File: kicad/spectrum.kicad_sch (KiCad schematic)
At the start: 258 parts, among them J1 SUPPLY, J2 Input, J3 Output, SW1 POWER, SW2 RIGHT SOURCE, SW3 LEFT SOURCE, U1 LM833, U10 LM833, U11 LM833, U12 LM833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

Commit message: Isolation transformer and resistor tweaks
- Audio isolation transformer to fix ground loop hum.
- Changed preamp Ri and mixer Rf to work compensate
  for transfomer effects.
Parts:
- added C51, C52: 0.1uF, Capacitor_THT:C_Disc_D4.3mm_W1.9mm_P5.00mm, symbol Device:C_Small
- added T1, T2: SP-70, symbol Device:Transformer_1P_1S
- R1, R126: value 1K -> 6.2K
- R54, R73: value 10K -> 51K
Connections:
- net GNDREF: now also C51.1, C52.1, T1.3 (SA), T2.4 (SB); no longer J2.S
- net Vin_L: now also T2.3 (SA); no longer J2.T
- net Vin_R: now also T1.4 (SB); no longer J2.R
- net at C50.2, R126.2: now also C52.2
- net at C1.2, R1.2: now also C51.2
- new net: J2.R, T1.1 (AA)
- new net: J2.S, T1.2 (AB), T2.1 (AA)
- new net: J2.T, T2.2 (AB)
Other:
- moved on the sheet: C1, C50, J2, TP2, TP27

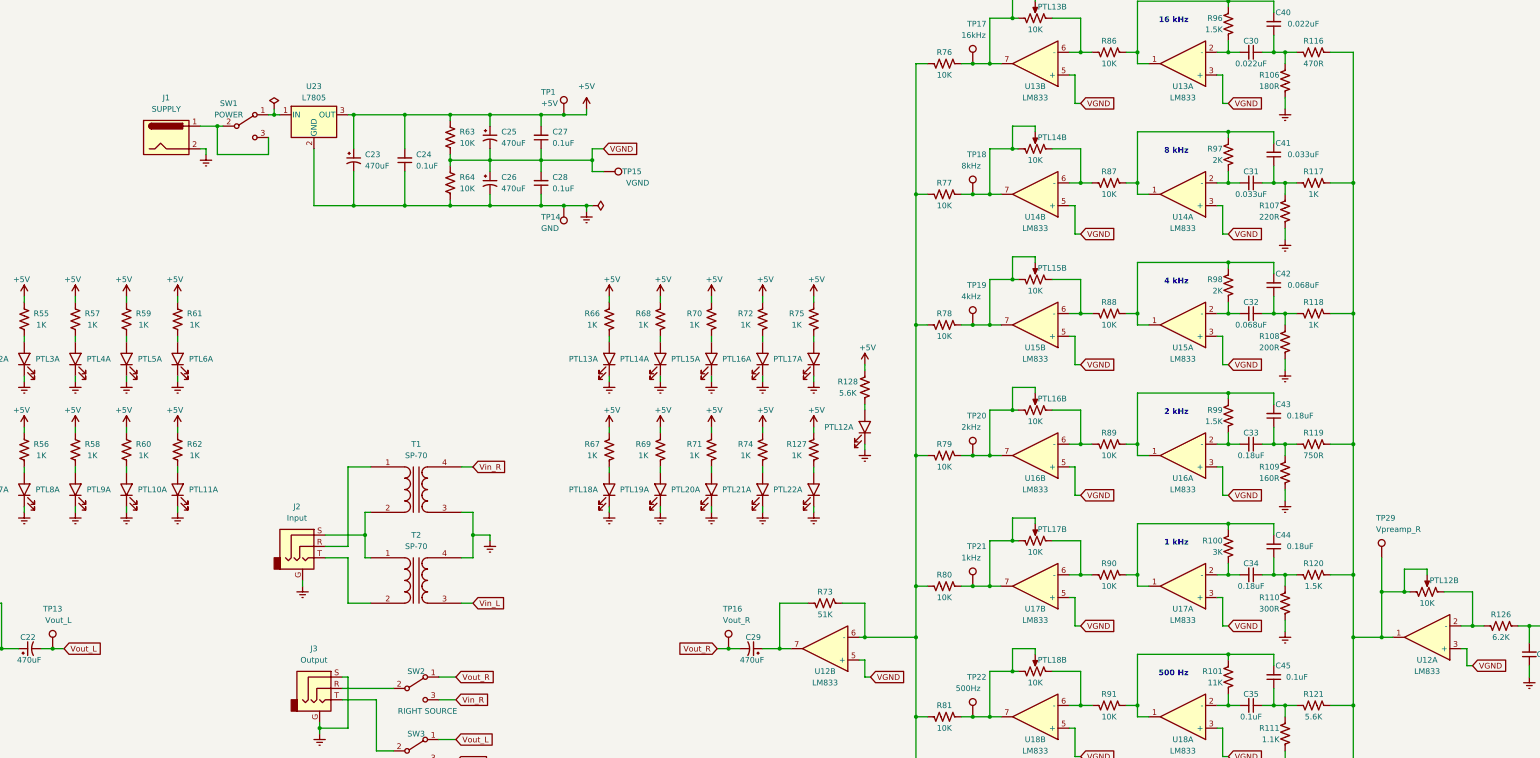
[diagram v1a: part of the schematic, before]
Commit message: Finish component layout and add extra 7805
- Extra 7805 needed for heat dissipation
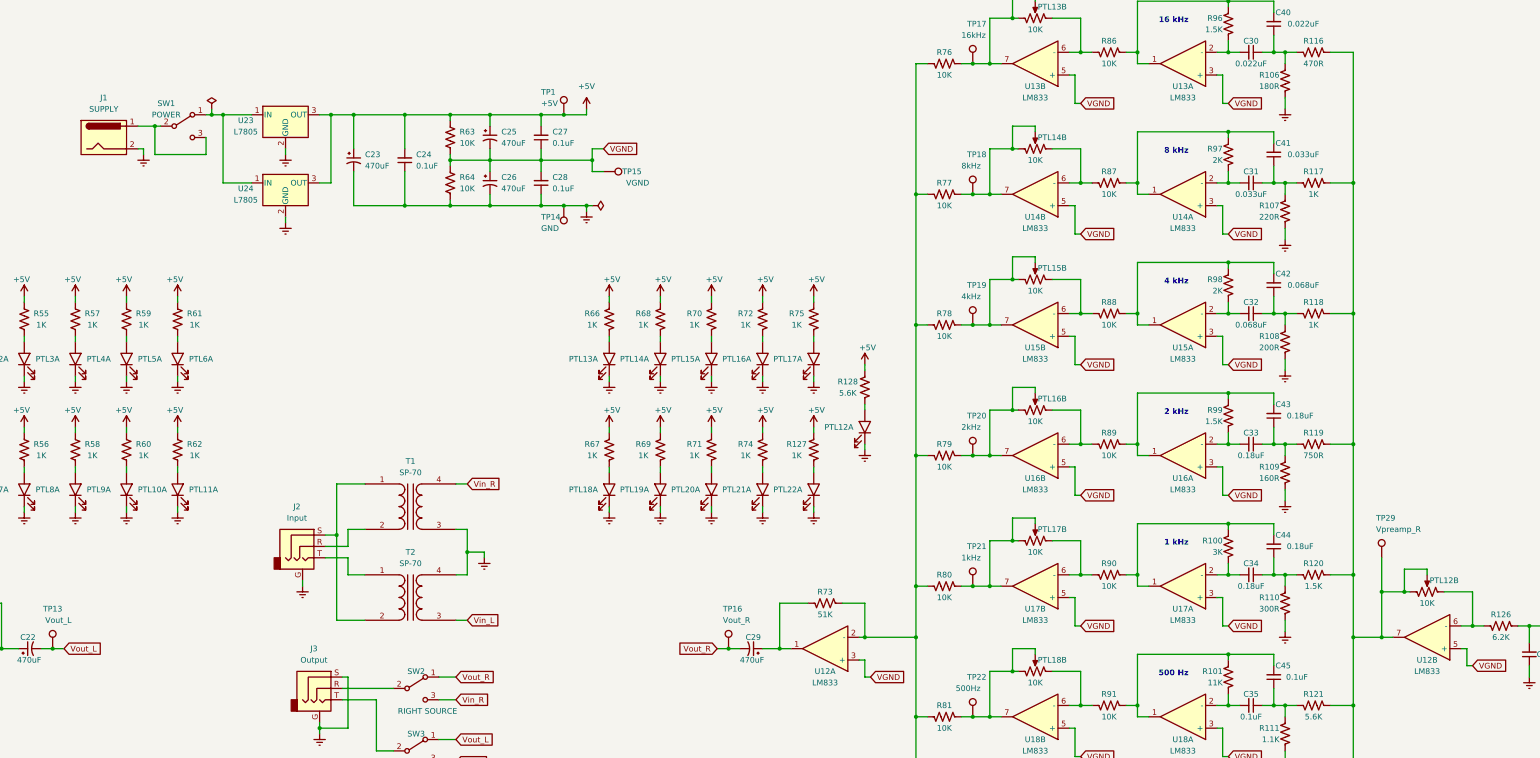
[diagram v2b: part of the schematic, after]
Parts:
- added U24: L7805, Package_TO_SOT_THT:TO-220-3_Vertical, symbol Regulator_Linear:L7805
- T1, T2: footprint (none) -> Triad_Magnetics_SP-70:SP70
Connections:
- net +5V: now also U24.3 (OUT)
- net GNDREF: now also U24.2 (GND)
- net VGND: now also U12.3 (+), U12.5 (+); no longer U12.3 (+), U12.5 (+)
- net at PTL12.2, PTL12.3, R116.2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: now also U12.7; no longer U12.1
- net at R73.2, R76.1, R77.1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: now also U12.2 (-); no longer U12.6 (-)
- net at J2.R: now also T1.2 (AB); no longer T1.1 (AA)
- net at T2.2 (AB): now also J2.S, T1.1 (AA); no longer J2.T
- net at PTL12.1, R126.1: now also U12.6 (-); no longer U12.2 (-)
- net at C29.1, R73.1: now also U12.1; no longer U12.7
- net at SW1.1 (A), U23.1 (IN): now also U24.1 (IN)
- new net: J2.T, T2.1 (AA)
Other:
- moved on the sheet: J1, SW1, T1, T2, U23

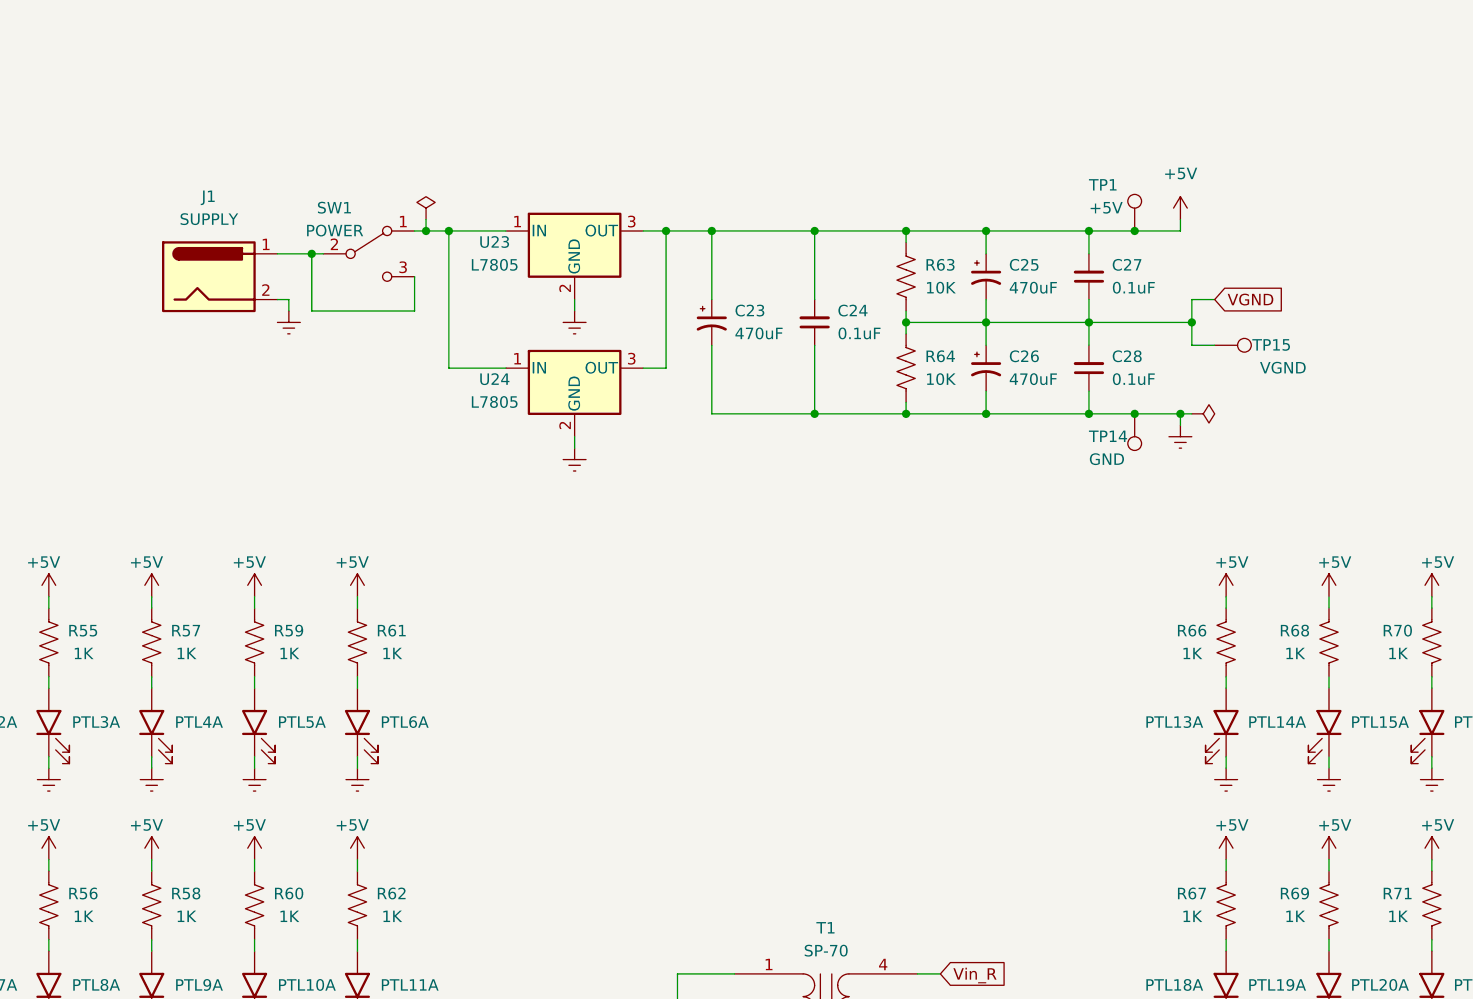
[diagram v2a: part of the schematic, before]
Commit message: Clean up board traces and use single L7805
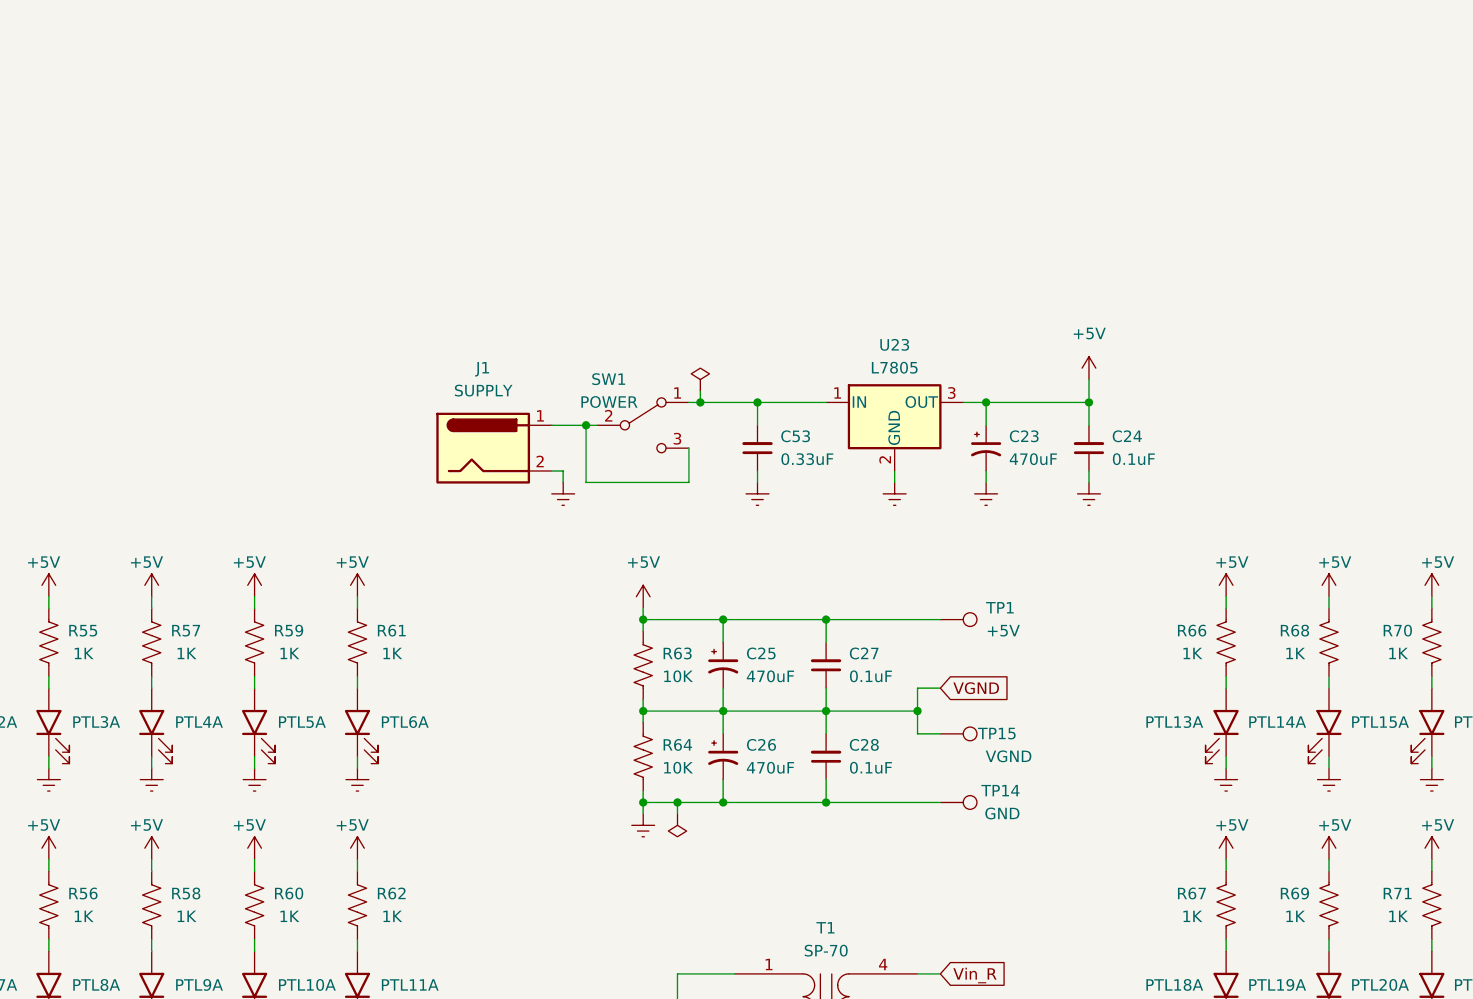
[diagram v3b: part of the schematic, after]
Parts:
- removed U24: L7805, Package_TO_SOT_THT:TO-220-3_Vertical, symbol Regulator_Linear:L7805
- added C53: 0.33uF, Capacitor_THT:C_Disc_D4.3mm_W1.9mm_P5.00mm, symbol Device:C_Small
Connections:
- net GNDREF: now also C53.1
- net at SW1.1 (A), U23.1 (IN): now also C53.2
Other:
- moved on the sheet: C23, C24, C25, C26, C27, C28, J1, R63, R64, SW1, TP1, TP14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

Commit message: Add output resistor to cut out noise
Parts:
- added R129, R130: 470R, Resistor_THT:R_Axial_DIN0207_L6.3mm_D2.5mm_P7.62mm_Horizontal, symbol Device:R_US
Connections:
- net Vout_L: now also R129.2; no longer C22.2
- net Vout_R: now also R130.1; no longer C29.2
- new net: C22.2, R129.1
- new net: C29.2, R130.2
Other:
- moved on the sheet: TP13, TP16
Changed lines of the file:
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@@
   (junction (at 303.53 153.67) (diameter 0) (color 0 0 0 0)
   )
+  (junction (at 233.68 209.55) (diameter 0) (color 0 0 0 0)
+  )
   (junction (at 496.57 163.83) (diameter 0) (color 0 0 0 0)
   )
@@
   (junction (at 132.08 222.25) (diameter 0) (color 0 0 0 0)
   )
-  (junction (at 374.65 209.55) (diameter 0) (color 0 0 0 0)
-  )
   (junction (at 144.78 280.67) (diameter 0) (color 0 0 0 0)
   )
@@
   (junction (at 283.21 143.51) (diameter 0) (color 0 0 0 0)
   )
-  (junction (at 223.52 209.55) (diameter 0) (color 0 0 0 0)
-  )
   (junction (at 466.09 163.83) (diameter 0) (color 0 0 0 0)
   )
@@
   (junction (at 57.15 204.47) (diameter 0) (color 0 0 0 0)
   )
+  (junction (at 364.49 209.55) (diameter 0) (color 0 0 0 0)
+  )
   (junction (at 433.07 224.79) (diameter 0) (color 0 0 0 0)
   )
@@
     (stroke (width 0) (type default) (color 0 0 0 0))
   )
+  (wire (pts (xy 233.68 209.55) (xy 231.14 209.55))
+    (stroke (width 0) (type default) (color 0 0 0 0))
+  )
   (wire (pts (xy 293.37 203.2) (xy 287.02 203.2))
     (stroke (width 0) (type default) (color 0 0 0 0))
@@
     (stroke (width 0) (type default) (color 0 0 0 0))
   )
-  (wire (pts (xy 374.65 209.55) (xy 372.11 209.55))
-    (stroke (width 0) (type default) (color 0 0 0 0))
-  )
   (wire (pts (xy 146.05 175.26) (xy 144.78 175.26))
     (stroke (width 0) (type default) (color 0 0 0 0))
@@
     (stroke (width 0) (type default) (color 0 0 0 0))
   )
-  (wire (pts (xy 220.98 209.55) (xy 223.52 209.55))
-    (stroke (width 0) (type default) (color 0 0 0 0))
-  )
   (wire (pts (xy 429.26 341.63) (xy 426.72 341.63))
     (stroke (width 0) (type default) (color 0 0 0 0))
@@
     (stroke (width 0) (type default) (color 0 0 0 0))
   )
+  (wire (pts (xy 364.49 209.55) (xy 361.95 209.55))
+    (stroke (width 0) (type default) (color 0 0 0 0))
+  )
   (wire (pts (xy 443.23 63.5) (xy 438.15 63.5))
     (stroke (width 0) (type default) (color 0 0 0 0))
@@
     (stroke (width 0) (type default) (color 0 0 0 0))
   )
+  (wire (pts (xy 364.49 209.55) (xy 367.03 209.55))
+    (stroke (width 0) (type default) (color 0 0 0 0))
+  )
   (wire (pts (xy 365.76 274.32) (xy 365.76 276.86))
     (stroke (width 0) (type default) (color 0 0 0 0))
@@
     (stroke (width 0) (type default) (color 0 0 0 0))
   )
+  (wire (pts (xy 233.68 209.55) (xy 236.22 209.55))
+    (stroke (width 0) (type default) (color 0 0 0 0))
+  )
   (wire (pts (xy 228.6 177.8) (xy 228.6 179.07))
     (stroke (width 0) (type default) (color 0 0 0 0))
@@
     (stroke (width 0) (type default) (color 0 0 0 0))
   )
-  (wire (pts (xy 223.52 209.55) (xy 226.06 209.55))
-    (stroke (width 0) (type default) (color 0 0 0 0))
-  )
   (wire (pts (xy 83.82 251.46) (xy 88.9 251.46))
     (stroke (width 0) (type default) (color 0 0 0 0))
@@
     (stroke (width 0) (type default) (color 0 0 0 0))
   )
+  (wire (pts (xy 374.65 209.55) (xy 377.19 209.55))
+    (stroke (width 0) (type default) (color 0 0 0 0))
+  )
   (wire (pts (xy 439.42 185.42) (xy 438.15 185.42))
     (stroke (width 0) (type default) (color 0 0 0 0))
@@
     (stroke (width 0) (type default) (color 0 0 0 0))
   )
-  (wire (pts (xy 377.19 209.55) (xy 374.65 209.55))
-    (stroke (width 0) (type default) (color 0 0 0 0))
-  )
   (wire (pts (xy 142.24 251.46) (xy 144.78 251.46))
     (stroke (width 0) (type default) (color 0 0 0 0))
@@
     (stroke (width 0) (type default) (color 0 0 0 0))
   )
+  (wire (pts (xy 220.98 209.55) (xy 223.52 209.55))
+    (stroke (width 0) (type default) (color 0 0 0 0))
+  )
   (wire (pts (xy 435.61 224.79) (xy 433.07 224.79))
     (stroke (width 0) (type default) (color 0 0 0 0))
@@
     )
   )
-  (global_label "Vout_L" (shape input) (at 226.06 209.55 0) (fields_autoplaced)
+  (global_label "Vout_L" (shape input) (at 236.22 209.55 0) (fields_autoplaced)
     (effects (font (size 1.27 1.27)) (justify left))
-    (property "Intersheet References" "${INTERSHEET_REFS}" (id 0) (at 234.5812 209.4706 0)
+    (property "Intersheet References" "${INTERSHEET_REFS}" (id 0) (at 244.7412 209.4706 0)
       (effects (font (size 1.27 1.27)) (justify left) hide)
     )
@@
     )
   )
-  (global_label "Vout_R" (shape input) (at 372.11 209.55 180) (fields_autoplaced)
+  (global_label "Vout_R" (shape input) (at 361.95 209.55 180) (fields_autoplaced)
     (effects (font (size 1.27 1.27)) (justify right))
-    (property "Intersheet References" "${INTERSHEET_REFS}" (id 0) (at 363.3469 209.4706 0)
+    (property "Intersheet References" "${INTERSHEET_REFS}" (id 0) (at 353.1869 209.4706 0)
       (effects (font (size 1.27 1.27)) (justify right) hide)
     )
@@
     (pin "2")
   )
+  (symbol (lib_id "Device:R_US") (at 370.84 209.55 90) (unit 1)
+    (in_bom yes) (on_board yes)
+    (property "Reference" "R130" (id 0) (at 370.84 207.01 90))
+    (property "Value" "470R" (id 1) (at 370.84 212.09 90))
+    (property "Footprint" "Resistor_THT:R_Axial_DIN0207_L6.3mm_D2.5mm_P7.62mm_Horizontal" (id 2) (at 371.094 208.534 90)
+      (effects (font (size 1.27 1.27)) hide)
+    )
+    (property "Datasheet" "~" (id 3) (at 370.84 209.55 0)
+      (effects (font (size 1.27 1.27)) hide)
+    )
+    (pin "1")
+    (pin "2")
+  )
   (symbol (lib_id "power:GNDREF") (at 374.65 294.64 0) (mirror y) (unit 1)
     (in_bom yes) (on_board yes) (fields_autoplaced)
@@
     (pin "8")
   )
+  (symbol (lib_id "Device:R_US") (at 227.33 209.55 90) (unit 1)
+    (in_bom yes) (on_board yes)
+    (property "Reference" "R129" (id 0) (at 227.33 207.01 90))
+    (property "Value" "470R" (id 1) (at 227.33 212.09 90))
+    (property "Footprint" "Resistor_THT:R_Axial_DIN0207_L6.3mm_D2.5mm_P7.62mm_Horizontal" (id 2) (at 227.584 208.534 90)
+      (effects (font (size 1.27 1.27)) hide)
+    )
+    (property "Datasheet" "~" (id 3) (at 227.33 209.55 0)
+      (effects (font (size 1.27 1.27)) hide)
+    )
+    (pin "1")
+    (pin "2")
+  )
   (symbol (lib_id "bourns_ptl:Bourns_PTL") (at 194.31 161.29 90) (unit 1)
     (in_bom yes) (on_board yes)
@@
     (pin "2")
   )
-  (symbol (lib_id "Connector:TestPoint") (at 374.65 209.55 0) (unit 1)
+  (symbol (lib_id "Connector:TestPoint") (at 364.49 209.55 0) (unit 1)
     (in_bom yes) (on_board yes)
-    (property "Reference" "TP16" (id 0) (at 373.38 200.66 0)
+    (property "Reference" "TP16" (id 0) (at 363.22 200.66 0)
       (effects (font (size 1.27 1.27)) (justify left))
     )
-    (property "Value" "Vout_R" (id 1) (at 373.38 203.2 0)
+    (property "Value" "Vout_R" (id 1) (at 363.22 203.2 0)
       (effects (font (size 1.27 1.27)) (justify left))
     )
-    (property "Footprint" "TestPoint:TestPoint_Keystone_5000-5004_Miniature" (id 2) (at 379.73 209.55 0)
+    (property "Footprint" "TestPoint:TestPoint_Keystone_5000-5004_Miniature" (id 2) (at 369.57 209.55 0)
       (effects (font (size 1.27 1.27)) hide)
     )
-    (property "Datasheet" "~" (id 3) (at 379.73 209.55 0)
+    (property "Datasheet" "~" (id 3) (at 369.57 209.55 0)
       (effects (font (size 1.27 1.27)) hide)
     )
@@
     (pin "1")
   )
-  (symbol (lib_id "Connector:TestPoint") (at 223.52 209.55 0) (unit 1)
+  (symbol (lib_id "Connector:TestPoint") (at 233.68 209.55 0) (unit 1)
     (in_bom yes) (on_board yes)
-    (property "Reference" "TP13" (id 0) (at 223.52 200.66 0))
-    (property "Value" "Vout_L" (id 1) (at 224.79 203.2 0))
-    (property "Footprint" "TestPoint:TestPoint_Keystone_5000-5004_Miniature" (id 2) (at 228.6 209.55 0)
+    (property "Reference" "TP13" (id 0) (at 233.68 200.66 0))
+    (property "Value" "Vout_L" (id 1) (at 234.95 203.2 0))
+    (property "Footprint" "TestPoint:TestPoint_Keystone_5000-5004_Miniature" (id 2) (at 238.76 209.55 0)
       (effects (font (size 1.27 1.27)) hide)
     )
-    (property "Datasheet" "~" (id 3) (at 228.6 209.55 0)
+    (property "Datasheet" "~" (id 3) (at 238.76 209.55 0)
       (effects (font (size 1.27 1.27)) hide)
     )
@@
       (reference "R128") (unit 1) (value "5.6K") (footprint "Resistor_THT:R_Axial_DIN0207_L6.3mm_D2.5mm_P7.62mm_Horizontal")
     )
+    (path "/98c493b0-58b5-49bc-a92a-f10022554972"
+      (reference "R129") (unit 1) (value "470R") (footprint "Resistor_THT:R_Axial_DIN0207_L6.3mm_D2.5mm_P7.62mm_Horizontal")
+    )
+    (path "/6d847187-e7f3-4c9c-aaaa-b31c47ee32e6"
+      (reference "R130") (unit 1) (value "470R") (footprint "Resistor_THT:R_Axial_DIN0207_L6.3mm_D2.5mm_P7.62mm_Horizontal")
+    )
     (path "/b58d0db8-9a2f-40d6-80cd-7939e1b77f51"
